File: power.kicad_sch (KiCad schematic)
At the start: 22 parts

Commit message: Terminal block part selections
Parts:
- removed J?: ACT ARMED, symbol Connector:Screw_Terminal_01x02
- removed J?: ACT DISARMED, symbol Connector:Screw_Terminal_01x02
- removed J?: ENERGIZE, symbol Connector:Screw_Terminal_01x02
- added J?: ENERGIZE, TerminalBlock_Phoenix:TerminalBlock_Phoenix_PT-1,5-2-5.0-H_1x02_P5.00mm_Horizontal, symbol Connector:Screw_Terminal_01x02
- added J?: ACT ARMED, TerminalBlock_Phoenix:TerminalBlock_Phoenix_PT-1,5-2-5.0-H_1x02_P5.00mm_Horizontal, symbol Connector:Screw_Terminal_01x02
- added J?: ACT DISARMED, TerminalBlock_Phoenix:TerminalBlock_Phoenix_PT-1,5-2-5.0-H_1x02_P5.00mm_Horizontal, symbol Connector:Screw_Terminal_01x02
- J?: MPN (none) -> 1773976
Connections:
- net GNDPWR: now also J?.2 (Pin_2), J?.2 (Pin_2)
- net VSAFE: now also J?.1 (Pin_1)
- net Vdrive: now also J?.1 (Pin_1)
- net at D?.2 (A), K?.2: now also J?.2 (Pin_2)
- net at U?.3: now also J?.1 (Pin_1)

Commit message: more notes, generate pdf
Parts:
- gave numbers to parts that had none: 22
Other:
- note added: "ARM must be high to allow the mechanical relay to turn on, so the C&C can perform safety checks before applying actuator power 12.2mA through NMOS when armed"
- note added: "I2C address is 1001xxx where xxx is determined by 8 ordering #s. Ranges from 0x48 to 0x4F"
- note added: "default EEPROM setting is semi-differential mode VREF=1.65 is supplied by TLI4971 AOUT=Vref+S*I where S is constant and I is current Sensitivity S depends on range determined by part #: ±50A is 24mV/A ±75A is 16mV/A"

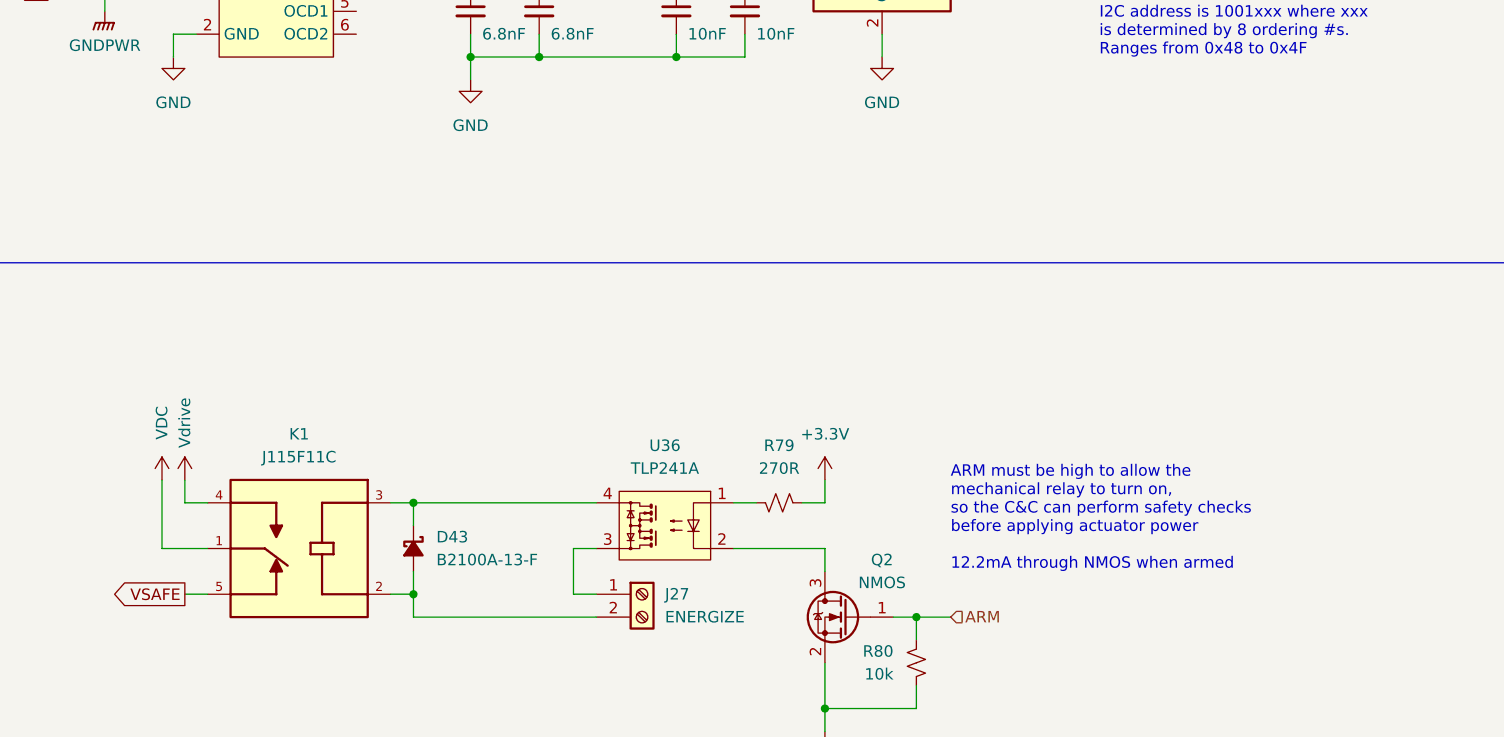
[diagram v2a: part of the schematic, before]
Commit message: estimate 3.3V current consumption
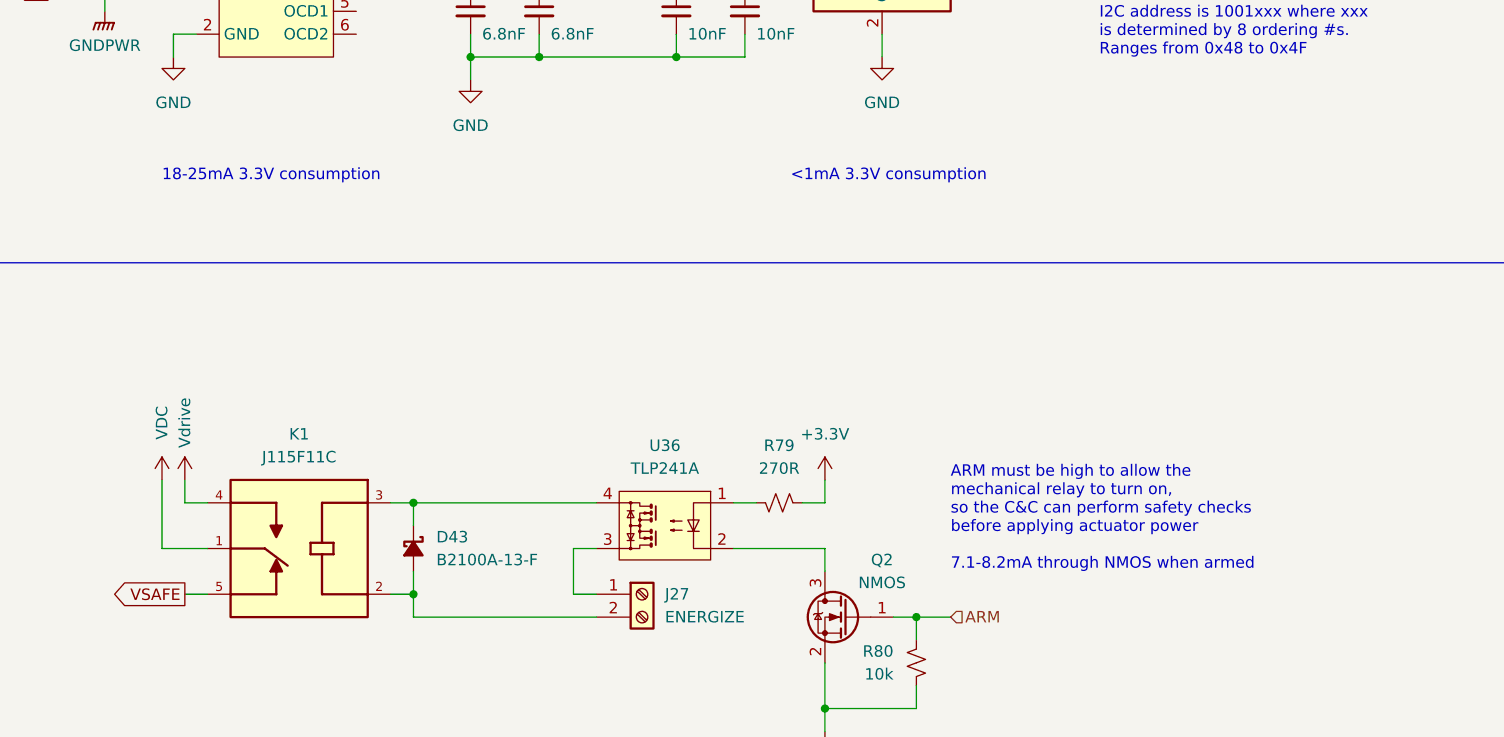
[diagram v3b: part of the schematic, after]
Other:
- note added: "18-25mA 3.3V consumption"
- note added: "<1mA 3.3V consumption"
- note added: "ARM must be high to allow the mechanical relay to turn on, so the C&C can perform safety checks before applying actuator power 7.1-8.2mA through NMOS when armed"
- note removed: "ARM must be high to allow the mechanical relay to turn on, so the C&C can perform safety checks before applying actuator power 12.2mA through NMOS when armed"

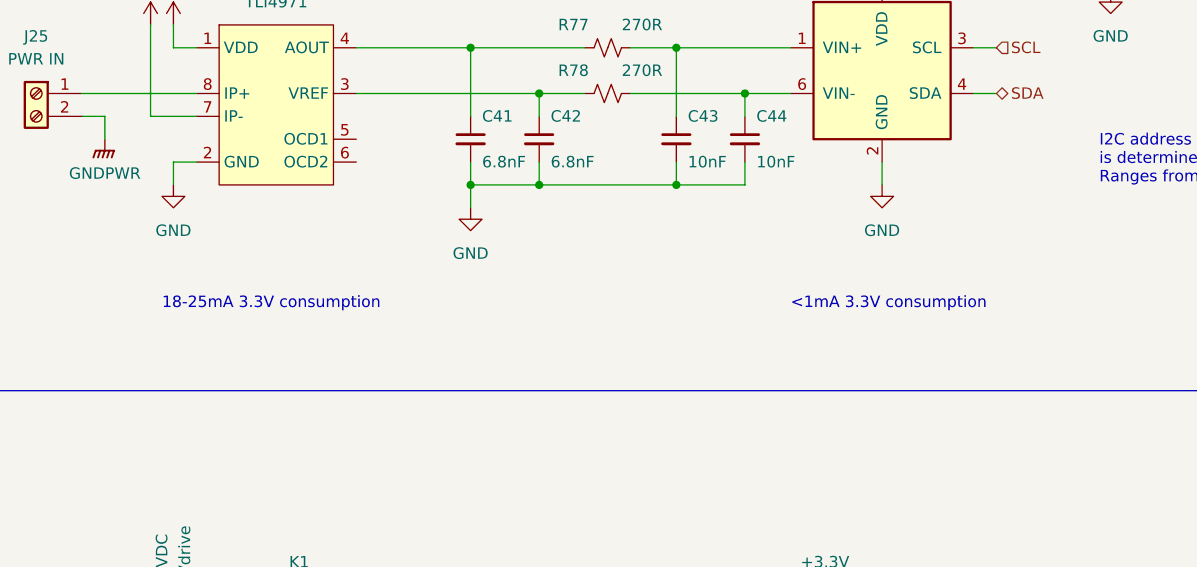
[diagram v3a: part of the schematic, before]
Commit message: labeled chips with their function
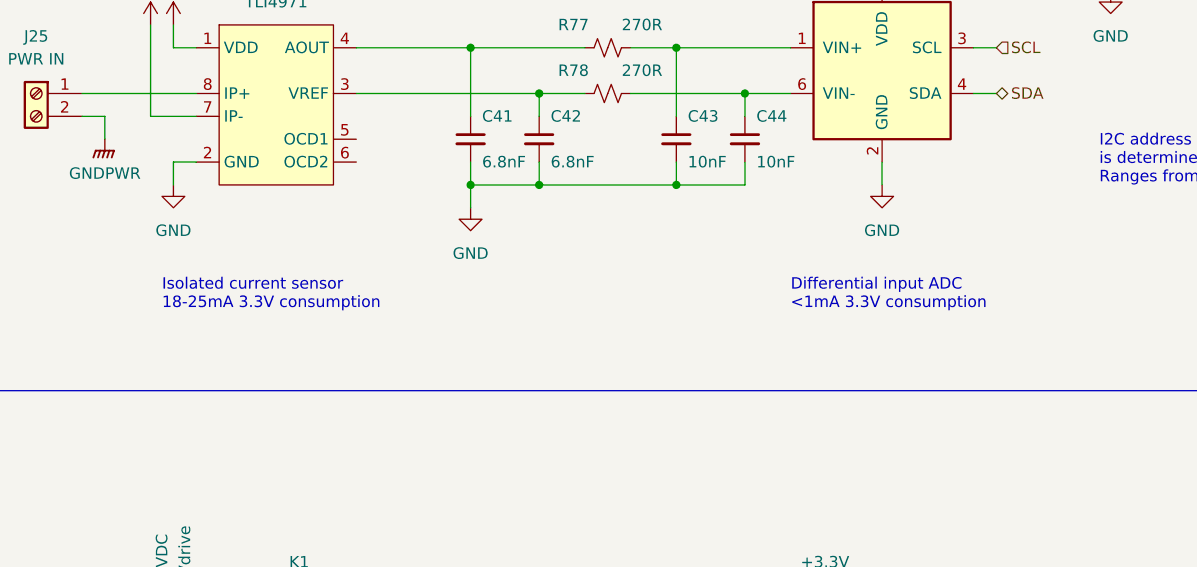
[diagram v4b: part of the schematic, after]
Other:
- note added: "Differential input ADC <1mA 3.3V consumption"
- note added: "Isolated current sensor 18-25mA 3.3V consumption"
- note removed: "18-25mA 3.3V consumption"
- note removed: "<1mA 3.3V consumption"

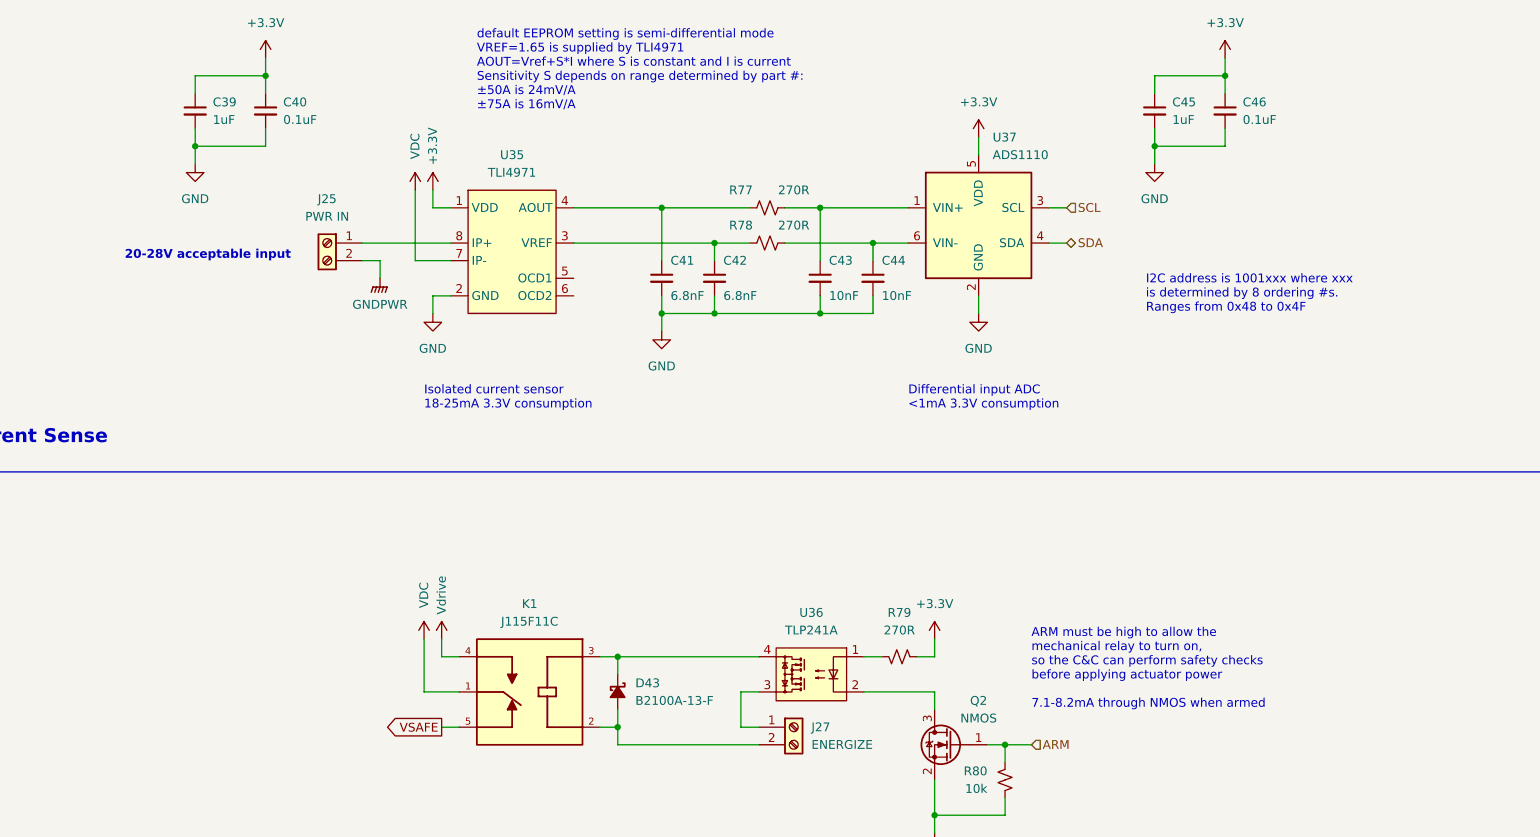
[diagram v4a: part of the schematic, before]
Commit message: Added feedback indicator LED buffer and made changes to notes
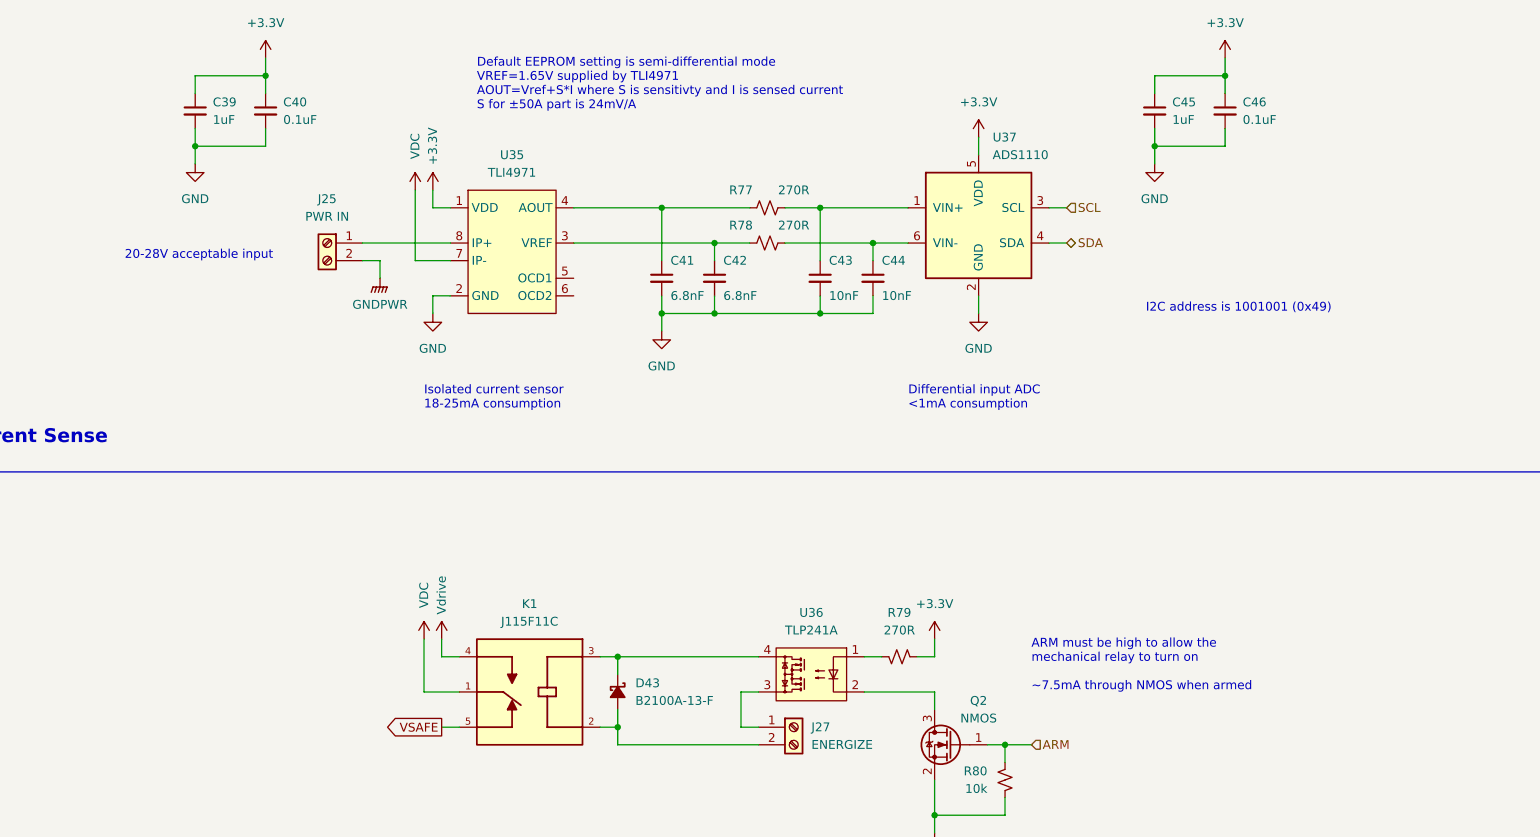
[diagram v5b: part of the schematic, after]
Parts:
- U37: MPN (none) -> ADS1110A1IDBVT
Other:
- note added: "ARM must be high to allow the mechanical relay to turn on ~7.5mA through NMOS when armed"
- note added: "Default EEPROM setting is semi-differential mode VREF=1.65V supplied by TLI4971 AOUT=Vref+S*I where S is sensitivty and I is sensed current S for ±50A part is 24mV/A"
- note added: "Differential input ADC <1mA consumption"
- note added: "I2C address is 1001001 (0x49)"
- note added: "Isolated current sensor 18-25mA consumption"
- note removed: "ARM must be high to allow the mechanical relay to turn on, so the C&C can perform safety checks before applying actuator power 7.1-8.2mA through NMOS when armed"
- note removed: "Differential input ADC <1mA 3.3V consumption"
- note removed: "I2C address is 1001xxx where xxx is determined by 8 ordering #s. Ranges from 0x48 to 0x4F"
- note removed: "Isolated current sensor 18-25mA 3.3V consumption"
- note removed: "default EEPROM setting is semi-differential mode VREF=1.65 is supplied by TLI4971 AOUT=Vref+S*I where S is constant and I is current Sensitivity S depends on range determined by part #: ±50A is 24mV/A ±75A is 16mV/A"
